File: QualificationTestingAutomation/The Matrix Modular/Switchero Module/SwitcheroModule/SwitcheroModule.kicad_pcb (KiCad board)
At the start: 4 copper layers, 87.5 x 78.9 mm, 93 parts, among them IC1 MAX3109ETJ+, J1 Conn_02x32_Counter_Clockwise_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, J2 OBD Connector, J3 OBD Connector, J6 Conn_02x32_Counter_Clockwise_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, Q1 2N7002DW, Q10 2N7002DW, Q2 2N7002DW, Q3 2N7002DW, Q4 2N7002DW, Q5 2N7002DW, Q6 2N7002DW, Q7 2N7002DW, Q8 2N7002DW, Q9 2N7002DW, SW1 SW_DIP_x04, U1 TC2050-JTAG-SchematicAutomati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, U10 TLP3546, U11 TLP3546, U12 CD4070B, U13 MAX324CUA, U14 CD4070B, U15 MAX324CUA, U2 AT25SF081-SSHD-X, U3 MSP430G2755IRHA40, U4 SN74HC266DR, U5 SN74LVC08APWR, U6 MAX14752, U7 DG408LE, U8 DS18B20_, U9 DS18B20_

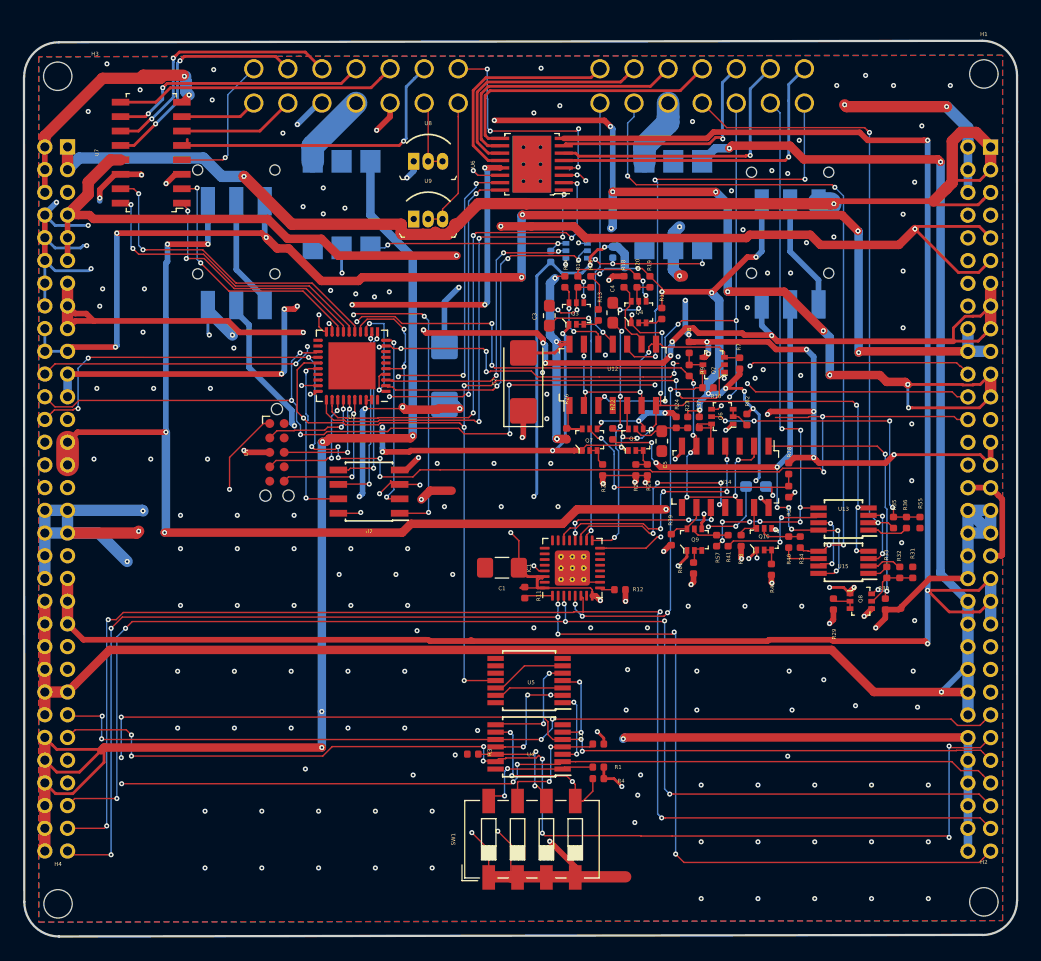
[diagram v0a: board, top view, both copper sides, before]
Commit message: Cleaned up the libraries Cleaned up the tracks Adjusted footprints to the manufacturers minimum size.
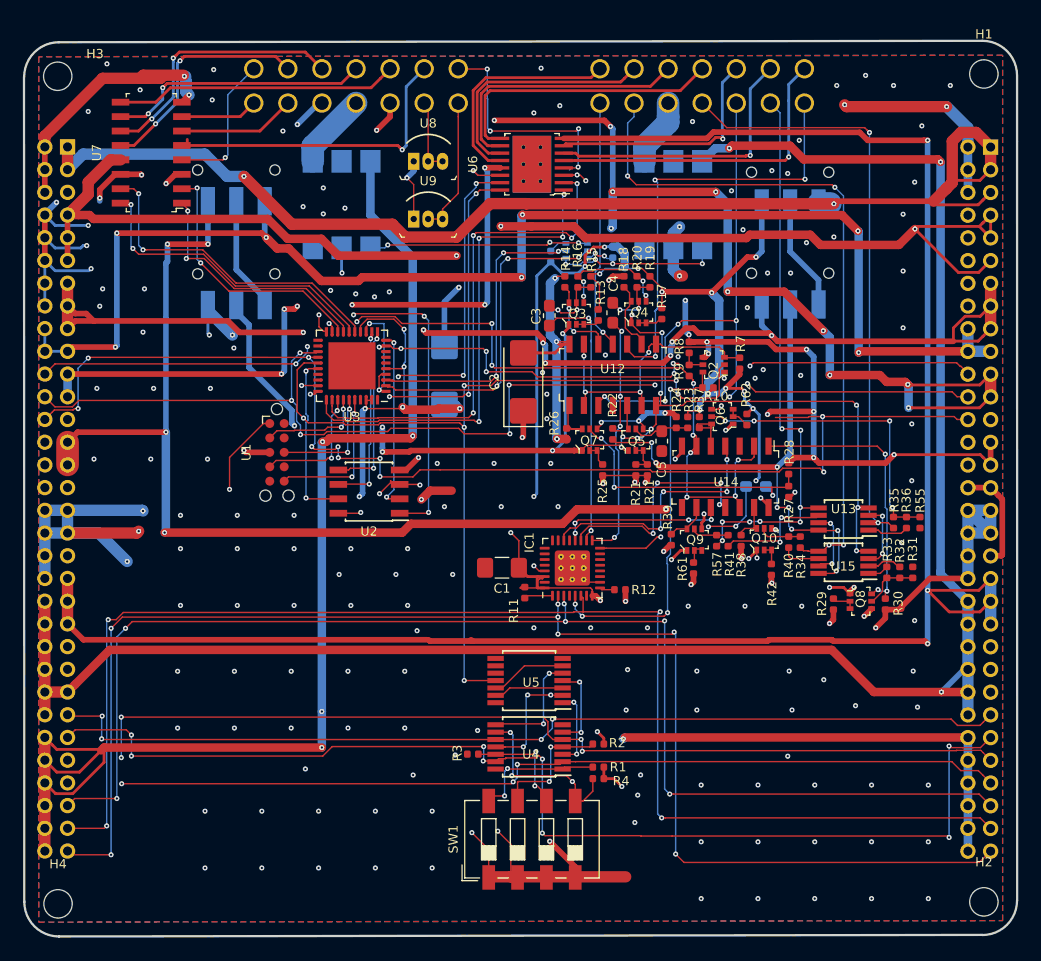
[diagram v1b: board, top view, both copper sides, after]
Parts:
- J1, J6: footprint Connector_PinHeader_2.00mm:PinHeader_2x32_P2.00mm_Horizontal -> Connector:PinHeader_2x32_P2.00mm_Horizontal
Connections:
- J1 pad 7: Net-(J1-Pad7) -> +12V
- J6 pad 45: Net-(J6-Pad45) -> GND
- J6 pad 47: Net-(J6-Pad47) -> GND
- J6 pad 49: VD -> GND
- Q1 pad 1: GND -> /Relays/1_RELH
- Q1 pad 3: /Relays/2_RELH -> Net-(Q1-Pad3)
- Q1 pad 4: GND -> /Relays/2_RELH
- Q1 pad 6: /Relays/1_RELH -> Net-(Q1-Pad6)
- R5 pad 2: /Relays/1_RELH -> Net-(Q1-Pad6)
- R6 pad 2: /Relays/2_RELH -> Net-(Q1-Pad3)
- U9 pad 1: Net-(U9-Pad1) -> GND
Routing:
- net +12V: track 108.0 -> 111.4 mm
- net /Relays/2_RELH: track 12.3 -> 15.0 mm, vias 3 -> 4
- net GND: track 114.8 -> 117.3 mm, vias 176 -> 174
- net Net-(Q1-Pad3): track 0.00 -> 2.39 mm, vias 0 -> 2
- net Net-(Q1-Pad6): track 0.00 -> 1.64 mm
- net /Relays/1_RELH: track 18.3 -> 19.5 mm, vias 2 -> 3
- net LO: track 107.3 -> 106.5 mm
- net 1_OUT1: track 27.1 -> 27.7 mm
- net 1_REL: track 29.5 -> 29.0 mm

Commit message: Added Voltage and current measurment of the muxes and relays to the MSP Some clean up of the tracks.
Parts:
- J1, J6: footprint Connector:PinHeader_2x32_P2.00mm_Horizontal -> Connector:PinHeader_2x32_P2.00mm_VerticalOpp
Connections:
- J1 pad 45: Net-(J1-Pad45) -> GND
- J1 pad 47: Net-(J1-Pad47) -> GND
- J1 pad 49: Net-(J1-Pad49) -> VD
- J6 pad 49: GND -> VD
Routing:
- net VDC: track 178.4 -> 229.4 mm
- net HT: track 141.4 -> 160.9 mm, vias 16 -> 13
- net LO: track 106.5 -> 100.5 mm
- net MOSI0: track 107.0 -> 102.8 mm
- net VAA: track 178.1 -> 174.1 mm
- net +5V: track 106.9 -> 103.0 mm
- net +1V8: track 109.7 -> 113.6 mm
- net GND: track 117.3 -> 113.5 mm
- net S2: track 100.8 -> 102.6 mm
- net Net-(U4-Pad3): track 6.93 -> 8.20 mm
- net +3V3: track 251.0 -> 252.2 mm
- net SSINV: track 33.8 -> 34.7 mm
- net S1: track 87.8 -> 88.7 mm
- net MOSI1: track 119.9 -> 119.1 mm
- net 1_ADC2: track 24.9 -> 25.7 mm
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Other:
- board text added: "-3V3"
- board text added: "-5V"
- board text added: "1V8"
- board text added: "3V3"
- board text added: "5V"
- board text added: "GND"

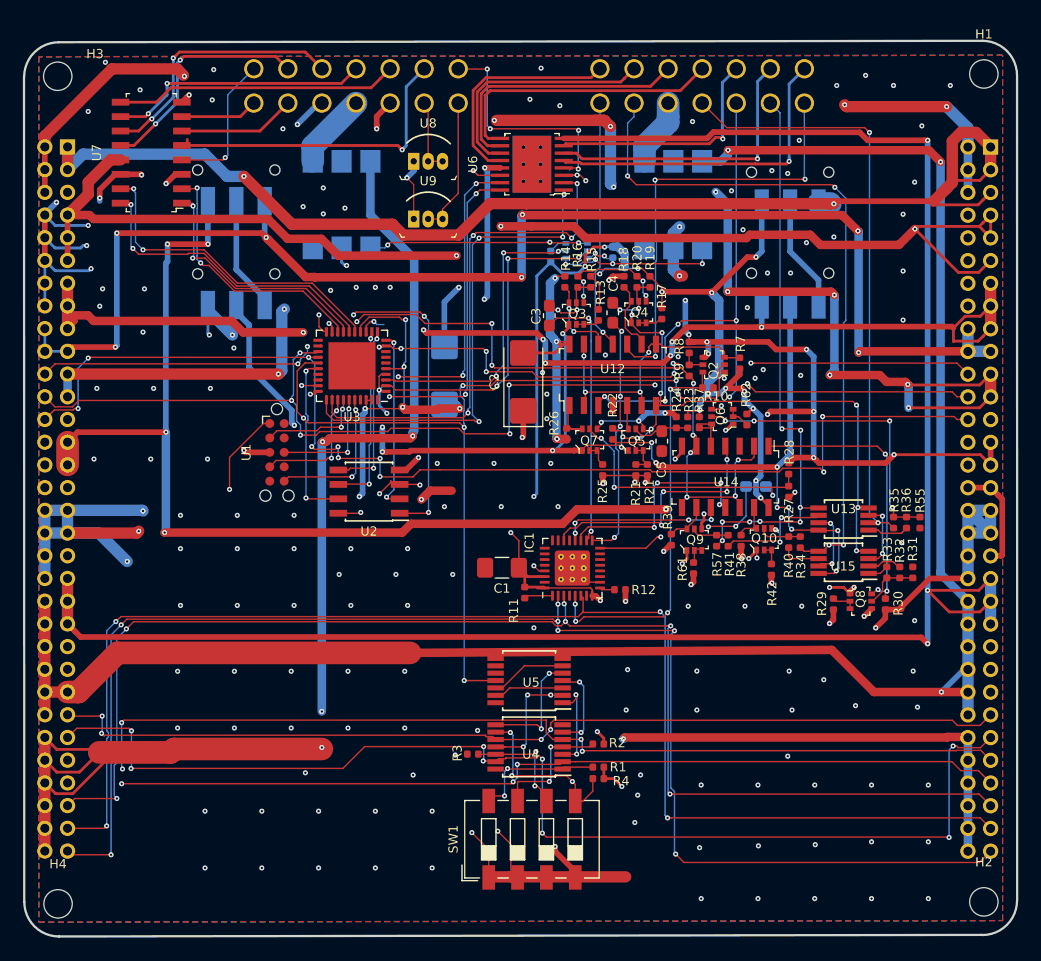
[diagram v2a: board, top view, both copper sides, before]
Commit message: Updated the layout to accomodate the voltage and current sensing.
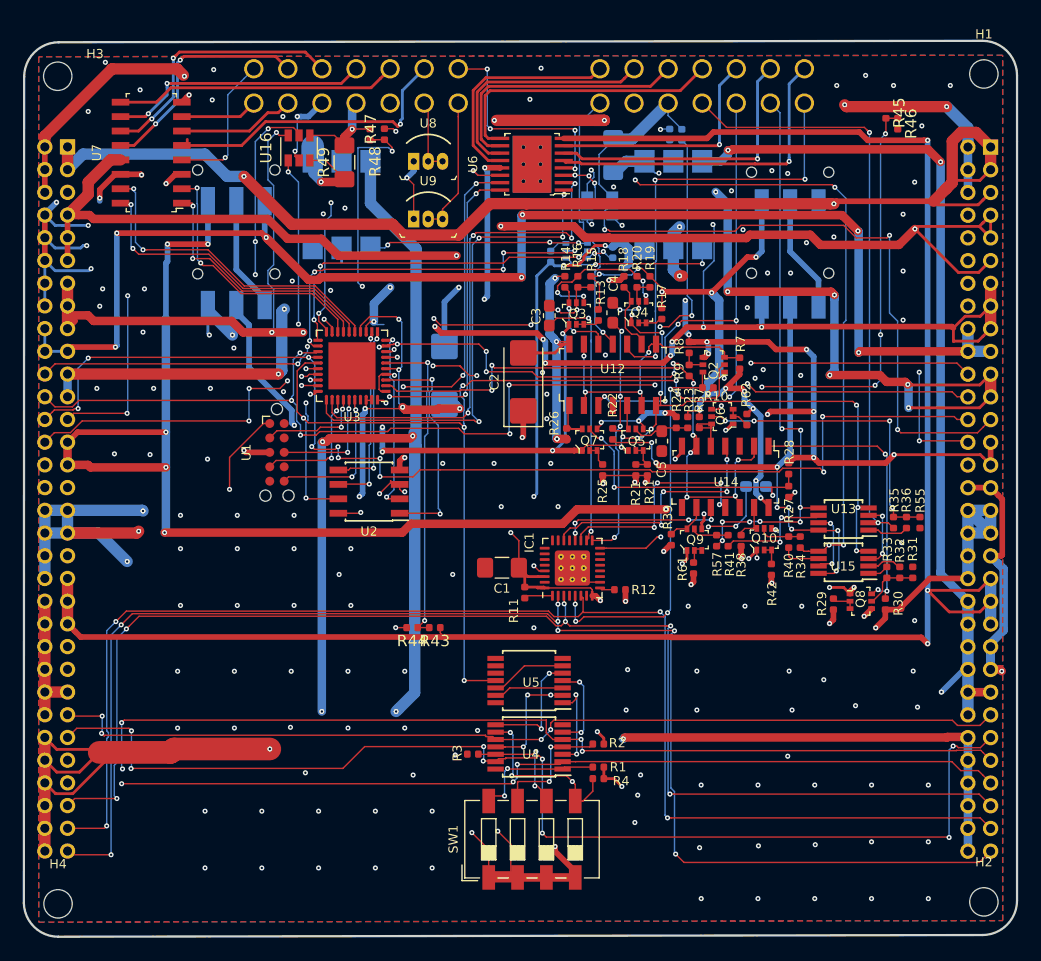
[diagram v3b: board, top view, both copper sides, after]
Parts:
- added R43: 1meg, Resistor_SMD:R_0402_1005Metric, F.Cu at (202.5, 70.3)
- added R44: 40K, Resistor_SMD:R_0402_1005Metric, F.Cu at (200.5, 70.3)
- added R45: 100k, Resistor_SMD:R_0402_1005Metric, F.Cu at (242.2, 24.9)
- added R46: 23.8K, Resistor_SMD:R_0402_1005Metric, F.Cu at (243.3, 25.9)
- added R47: 40K, Resistor_SMD:R_0402_1005Metric, F.Cu at (198.1, 26.8)
- added R48: 1meg, Resistor_SMD:R_0402_1005Metric, F.Cu at (196.8, 26.8)
- added R49: .02, Resistor_SMD:R_1206_3216Metric_Pad1.42x1.75mm_HandSolder, F.Cu at (194.6, 29.3)
- added R50: 40K, Resistor_SMD:R_0402_1005Metric, B.Cu at (223.2, 26.8)
- added R51: 1meg, Resistor_SMD:R_0402_1005Metric, B.Cu at (224.3, 26.9)
- added R52: .02, Resistor_SMD:R_1206_3216Metric_Pad1.42x1.75mm_HandSolder, B.Cu at (218.2, 28.7)
- added U16: INA181, Package_TO_SOT_SMD:SOT-23-6, F.Cu at (190.6, 28.0)
- added U17: INA181, Package_TO_SOT_SMD:SOT-23-6, B.Cu at (217.0, 33.1)
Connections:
- J1 pad 25: Net-(J1-Pad25) -> 1.25V
- J1 pad 28: GND -> +2V5
- J6 pad 25: Net-(J6-Pad25) -> 1.25V
- J6 pad 28: Net-(J6-Pad28) -> +2V5
- U10 pad 4: 1_Vin -> Net-(R49-Pad1)
- U11 pad 4: 1_GarminPWR -> Net-(R52-Pad1)
- U3 pad 19: RS232INV -> A4
- U3 pad 2: 1_REL -> RS232INV
- U3 pad 20: /Micro/CSB -> A3
- U3 pad 21: Net-(U3-Pad21) -> 1_REL
- U3 pad 22: Net-(U3-Pad22) -> 2_REL
- U3 pad 26: /Micro/\HOLD -> A5
- U3 pad 27: A3 -> GND
- U3 pad 28: A4 -> +2V5
- U3 pad 3: 2_REL -> /Micro/CSB
- U3 pad 40: 3_REL -> /Micro/\HOLD
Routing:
- net 1.25V: track 0.00 -> 131.6 mm, vias 0 -> 8
- net +2V5: track 0.00 -> 93.3 mm, vias 0 -> 6
- net A1: track 0.00 -> 70.3 mm, vias 0 -> 7
- net A4: track 0.00 -> 52.3 mm, vias 0 -> 5
- net +5V: track 103.0 -> 141.9 mm, vias 7 -> 12
- net A3: track 0.00 -> 36.7 mm, vias 0 -> 3
- net A5: track 0.00 -> 34.5 mm, vias 0 -> 4
- net A0: track 0.00 -> 28.4 mm, vias 0 -> 2
- net A2: track 0.00 -> 24.9 mm, vias 0 -> 3
- net GND: track 113.5 -> 138.4 mm, vias 174 -> 167
- net Net-(R52-Pad1): track 0.00 -> 13.4 mm, vias 0 -> 2
- net -3V3: track 197.6 -> 209.5 mm, vias 21 -> 22
- net /Micro/CSB: track 31.5 -> 20.0 mm, vias 4 -> 2
- net +3V3: track 252.2 -> 242.8 mm, vias 45 -> 44
- net Net-(R49-Pad1): track 0.00 -> 9.33 mm, vias 0 -> 1
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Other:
- outline, holes or cut-outs redrawn

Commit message: Schematic Clean ups the layout needs to be changed
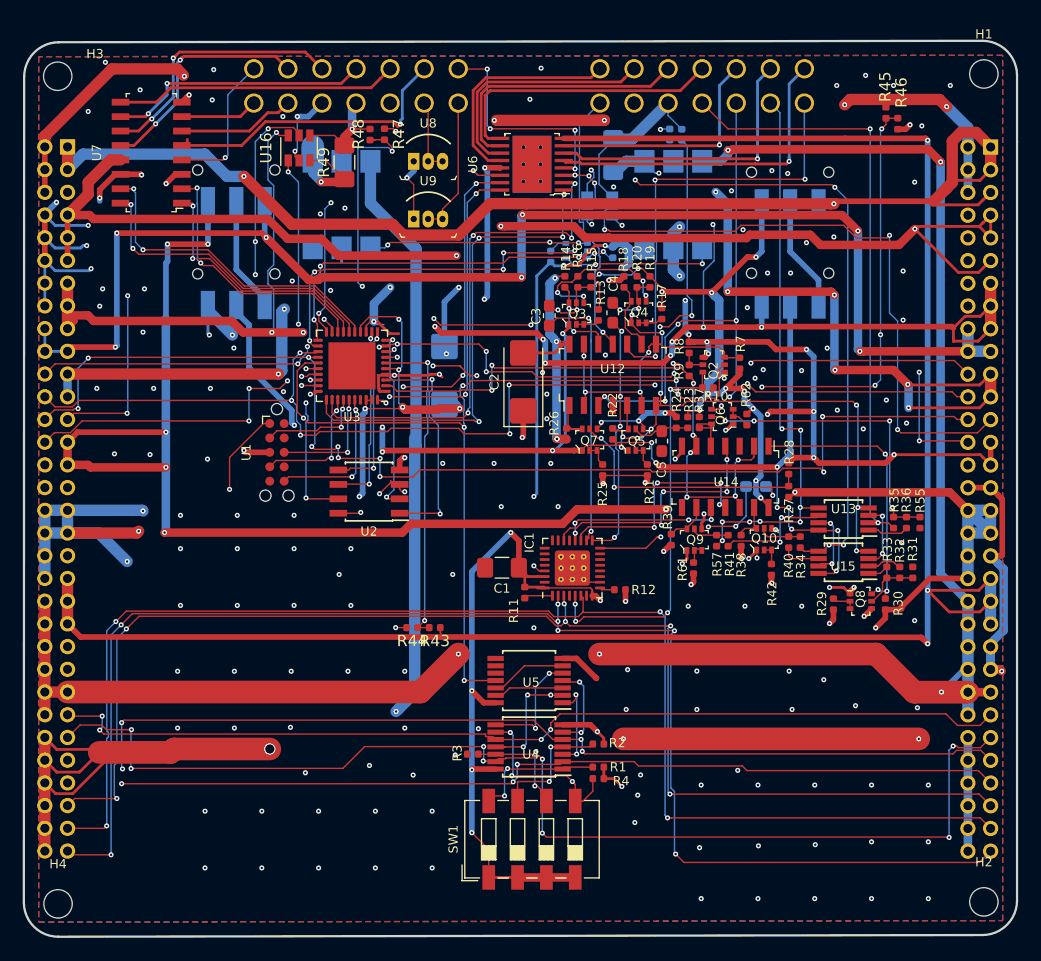
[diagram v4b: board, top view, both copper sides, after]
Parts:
- removed the R21 at (220.2, 56.4)
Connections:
- U4 pad 14: Net-(U4-Pad14) -> +3V3
- U4 pad 7: Net-(U4-Pad7) -> GND
- U5 pad 14: Net-(U5-Pad14) -> +3V3
- U5 pad 7: Net-(U5-Pad7) -> GND
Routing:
- net VDC: track 235.4 -> 172.9 mm, vias 6 -> 4
- net +3V3: track 242.8 -> 283.1 mm, vias 44 -> 43
- net GND: track 138.4 -> 157.0 mm, vias 167 -> 174
- net VD: track 171.0 -> 176.7 mm, vias 3 -> 5
- net LO: track 100.8 -> 101.9 mm
- net Net-(Q5-Pad2): track 3.05 -> 2.03 mm
- net HT: track 160.2 -> 159.3 mm
- net S3: track 84.9 -> 85.4 mm
- net (no net): vias 3 -> 2

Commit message: IO clean up added the 1v25 reference to Matrix Changed Some of the labels to more legible names.
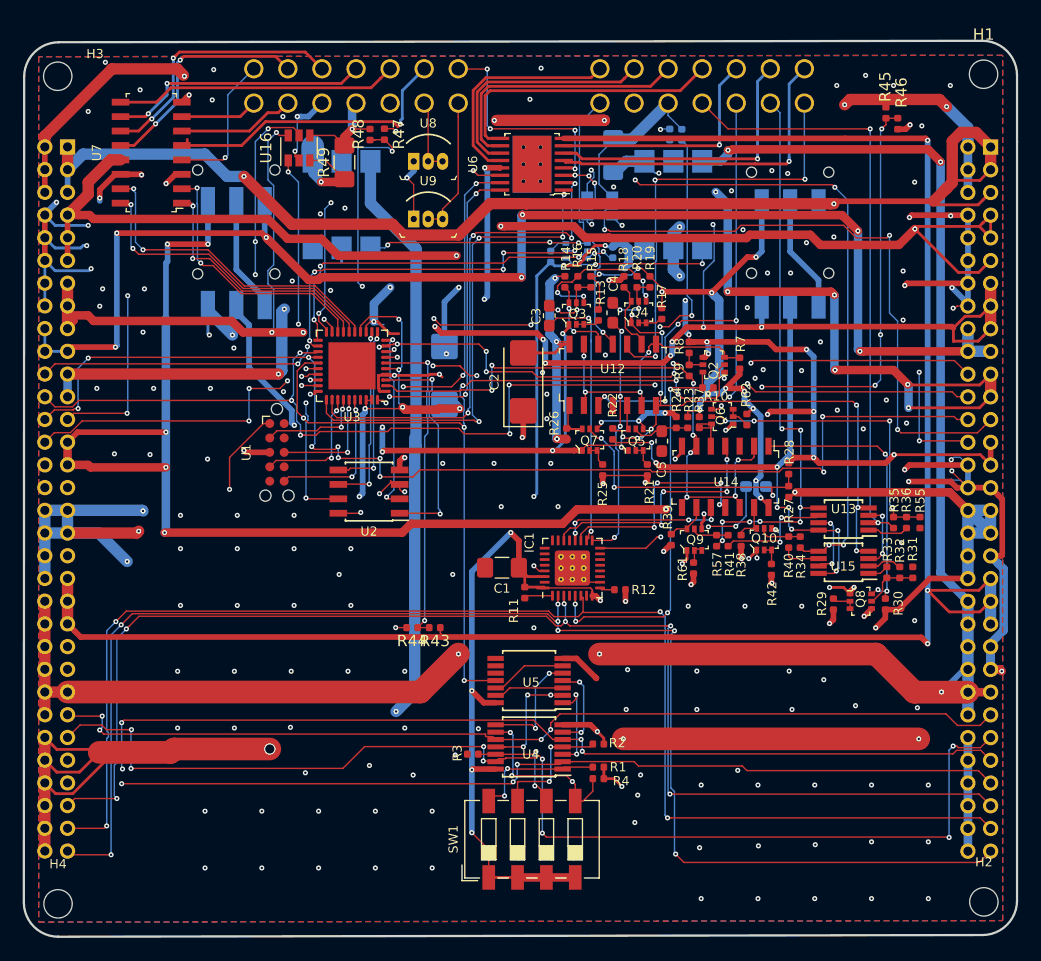
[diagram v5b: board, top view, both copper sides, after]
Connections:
- J6 pad 5: Net-(J6-Pad5) -> +1V8
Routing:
- net GND: track 157.0 -> 199.9 mm, vias 174 -> 183
- net +1V8: track 113.6 -> 115.6 mm
